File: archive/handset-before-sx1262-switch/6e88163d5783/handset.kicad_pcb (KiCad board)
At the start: 4 copper layers, 66 x 142 mm, 281 parts, among them J1 2053380002, J10 LF_COIL_TUNING_REQUIRED, J16 EXPANSION_J16, J2 PACK_NTC_10K_B3435, J20 LORA_915_ANT, J21 CC1101_915_ANT, J22 GNSS_PASSIVE_ANT, J23 DM3D-SF, J24 TSAL6400_CASE_LED, J25 TSOP38438_CASE_RX, J26 FH12A-50S-0.5SH(55), J3 MEDIA_SPEAKER_DIFFERENTIAL, J4 CALL_AUDIO_FROM_MODEM_ADAPTER, J5 CALL_EARPIECE, J6 CALL_MIC, J7 PIM447_HARNESS_VERIFY, J8 MODEM_ADAPTER_3V3_LOGIC, J9 MODEM_POWER_ADAPTER_REQUIRED, Q1 AO3400A, Q3 AO3400A, Q4 AO3400A, Q5 AO3400A, Q6 AO3401A, Q7 AO3400A, Q8 AO3400A, SW1 1, SW10 10, SW11 11, SW12 12, SW13 13, SW14 14, SW15 15, SW16 16, SW17 MCU_BOOT, SW18 MCU_EN, SW19 POWER, SW2 2, SW3 3, SW4 4, SW5 5, SW6 6, SW7 7, SW8 8, SW9 9, U1 ESP32-S3-WROOM-1-N16R8, U10 TPS61023DRLR, U11 TPS62840DLCR, U12 MAX-M10S-00B-01, U13 ST25R3916B-AQET, U14 TPS2553DBVR, U15 TPD4E05U06DQAR, U16 TPD4E05U06DQAR, U17 TPD4E05U06DQAR, U18 SN74AHCT125PWR, U19 SN74LVC1G17DBVR, U2 TCA8418RTWR, U20 TPS63070RNMR, U21 TPS25200DRVR, U22 TUSB320LAIRWBR, U23 TLV70433DBVR, U24 TCA9536DGKR, U25 STM32G031G8U6, U26 TPS7A0230PDBVR, U27 TCA9800DGKR, U28 TPS7A2030PDBVR, U29 SN74LVC244APWR, U3 BQ25186DLHR, U30 SN74LVC2G125DCUR, U31 TCA9406DCUR, U32 CAT4004AHU2-GT3, U33 TCA9537DGSR, U34 SN74CB3Q3245PWR, U35 SN74HCS10PWR, U36 0900FM15K0039001E, U37 BGS12WN6E6327, U4 SX1262IMLTRT, U5 CC1101RGPR, U6 MAX98357AETE+, U7 TPS63802DLAR, U8 MAX17048G+T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

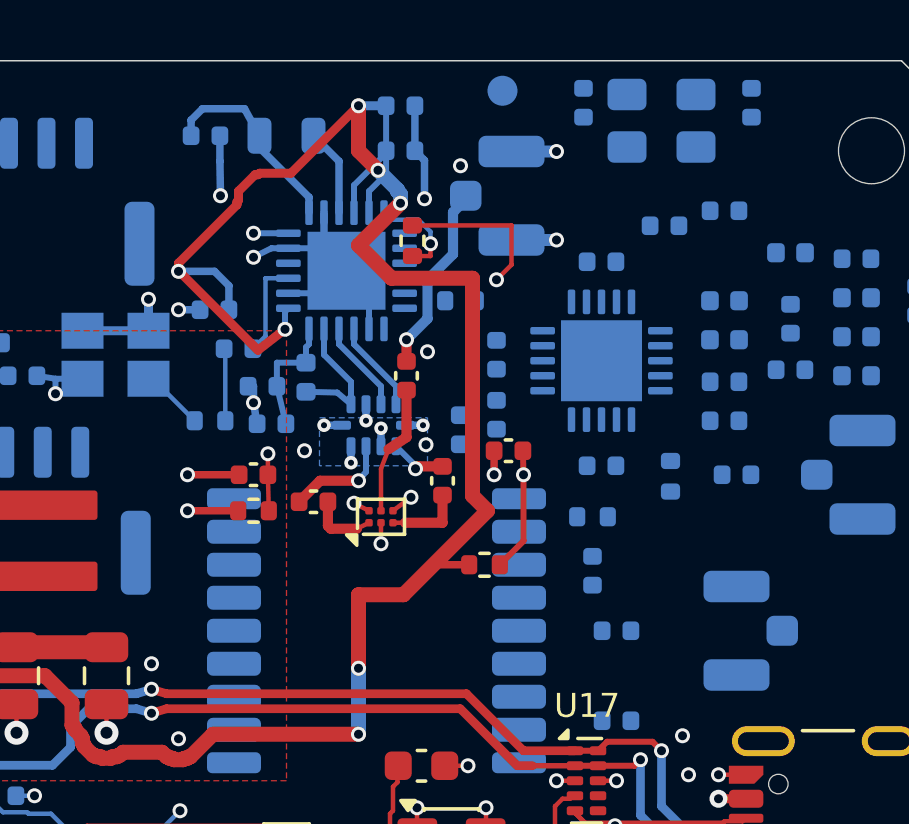
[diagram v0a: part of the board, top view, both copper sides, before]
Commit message: feat: route SX1262 switch and antenna path
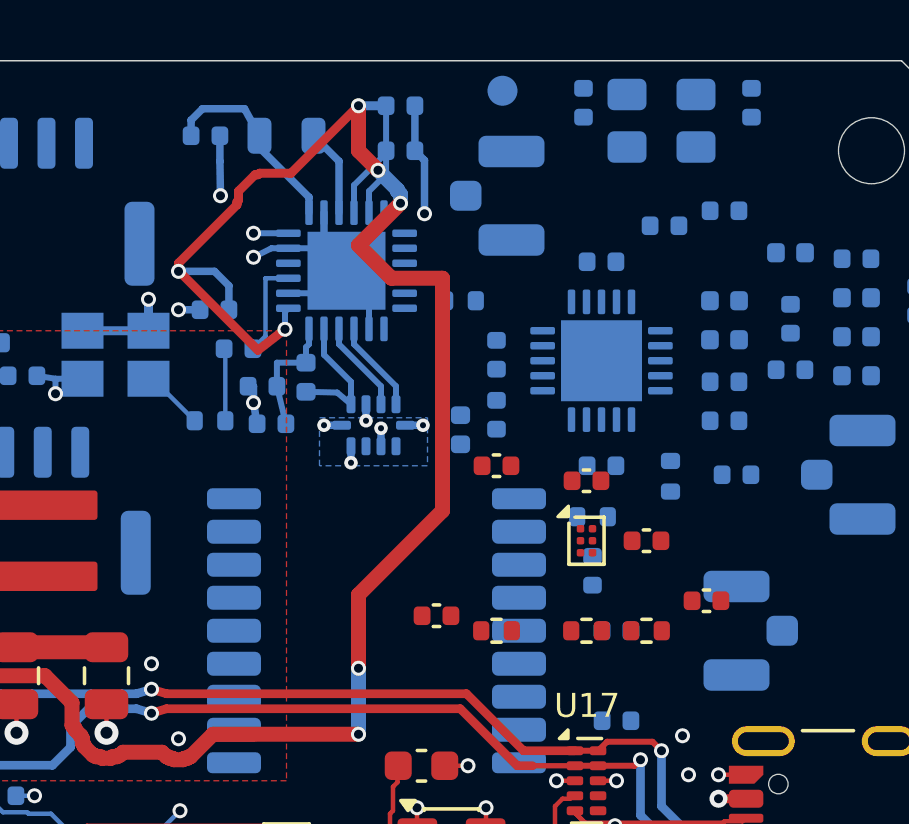
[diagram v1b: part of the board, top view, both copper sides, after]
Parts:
- moved R93 13.7 mm to (123.0, 48.0), turned to 0 degrees
- moved R91 13.3 mm to (118.0, 48.0), turned to 0 degrees
- moved C98 9.71 mm to (123.0, 45.0), turned to 0 degrees
- moved C97 8.28 mm to (125.0, 47.0), turned to 0 degrees
- moved C96 7.70 mm to (116.0, 47.5), turned to 0 degrees
- moved U37 6.90 mm to (121.0, 45.0), turned to 0 degrees
- moved C99 6.22 mm to (118.0, 42.5)
- moved C100 4.80 mm to (121.0, 43.0), turned to 0 degrees
- moved R92 4.05 mm to (121.0, 48.0)
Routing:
- net SX_SWITCH_CTRL: track 27.8 -> 0.00 mm, vias 3 -> 0
- net SX_SWITCH_VDD: track 10.0 -> 0.00 mm, vias 2 -> 0
- net GND: track 424.6 -> 417.2 mm, vias 193 -> 183
- net LORA_RF_50R: track 6.34 -> 0.00 mm, vias 1 -> 0
- net SX_ANT_AC: track 4.39 -> 0.00 mm
- net +3V3: track 503.2 -> 499.3 mm
- net SX_TX_MATCH: track 3.51 -> 0.00 mm, vias 1 -> 0
- net SX_RF_SW: track 3.36 -> 0.00 mm, vias 1 -> 0
- net SX_RX_AC: track 2.57 -> 0.00 mm
- net SX_TX_AC: track 2.26 -> 0.00 mm
- net SX_RX_MATCH: track 1.95 -> 0.00 mm, vias 1 -> 0
